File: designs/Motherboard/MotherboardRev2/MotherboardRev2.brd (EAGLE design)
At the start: 160 x 100 mm, 102 parts, among them IC1 PIC24FJ64GB202, IC2 PIC18F26J53SO, J1 Servo 2, J2 Servo 1, J3 Servo 3, J4 Servo 4, J5 Servo 5, J6 Servo 6, Q1 BSS123, Q2 BSS123, Q3 BSS123, Q4 BSS123, U3 LMS8117AMP-3.3

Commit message: More work done on motherboard
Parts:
- removed IC2: PIC18F26J53SO, microchip:SO28W
- removed J1: Servo 2, con-molex:7395-03
- removed J2: Servo 1, con-molex:7395-03
- removed J3: Servo 3, con-molex:7395-03
- removed J4: Servo 4, con-molex:7395-03
- removed J5: Servo 5, con-molex:7395-03
- removed J6: Servo 6, con-molex:7395-03
- added 3.3V, 3.3V(2), 5V, 5V(2): (no value), Son_of_Dark_Powersch:7395-02
- added C33: 10uF, rcl:C0805
- added C34, C35, C36: .1uF, rcl:C0805
- added C37: .1uF, 3-3_fixed:1206
- added C38: 10uF, SparkFun-Capacitors:EIA3216
- added D7: 3_3V_PWR, SparkFun-LED:FKIT-LED-1206
- added D8: 6V_Pwr, SparkFun-LED:FKIT-LED-1206
- added IC3: PIC24FJ64GB202, microchip:QFN28-ML_6X6MM
- added LED10, LED11, LED12: (no value), motherboard_i_autoroute:LED_CHIPLED_1206
- added MOTOR_PWR: (no value), Son_of_Dark_Powersch:7395-04
- added PWR_IN, PWR_IN(2): (no value), Son_of_Dark_Powersch:5569-2
- added R18: 470, rcl:R0805
- added R26: 10k, rcl:R0805
- added R27, R28: 4.7k, rcl:R0805
- added R29, R30, R31: (no value), rcl:M0805
- added R32: 0 ohm, rcl:R1206
- added R33: 4.7K, rcl:R0805
- added R34, R35: (no value), rcl:R0805W
- added SERVO_1, SERVO_10, SERVO_2, SERVO_3, SERVO_4, SERVO_5, SERVO_6, SERVO_7, SERVO_8, SERVO_9: (no value), con-molex:7395-03
- added START_SWITCH: (no value), con-lstb:MA03-1
- added U$10: Switch3, Parts4Class:MC32882_FINAL
- added U$11, U$13, U$14: Switch1, Parts4Class:MC32882_FINAL
- added U$12: Switch2, Parts4Class:MC32882_FINAL
- added U1: LMS8117AMP-3.3, NSC-LMS8117AMP:SOT230P696X180-4N
- C29: value .1uF -> 10uF; device 3-3_fixed:1206 -> SparkFun-Capacitors:EIA3216
- IC1: device microchip:DIL28-3 -> microchip:QFN28-ML_6X6MM
- R17: value 0 ohm -> 4.7K; device rcl:R1206 -> rcl:R0805
- moved R17 371.5 mm to (96.4, 51.1), flipped to the bottom, turned to 270 degrees
- moved C29 351.8 mm to (74.6, 76.9), flipped to the bottom, turned to 90 degrees
- moved PROGRAMMING 256.8 mm to (30.8, 3.73), flipped to the bottom, turned to 0 degrees
- moved D5 227.0 mm to (70.7, 65.7), flipped to the bottom
- moved R15 223.6 mm to (72.4, 61.5), flipped to the bottom
- moved U$5 220.3 mm to (51.8, 14.2), turned to 0 degrees
- moved C24 219.9 mm to (74.2, 65.6), flipped to the bottom
- moved IC1 216.2 mm to (73.3, 47.4), flipped to the bottom
- moved R21 212.7 mm to (94.5, 37.0)
- moved LED5 212.7 mm to (94.3, 31.3)
- moved R22 212.5 mm to (92.4, 37.0)
- moved LED9 212.5 mm to (86.2, 31.3)
- moved R23 212.5 mm to (90.3, 37.0)
- moved R24 212.5 mm to (88.3, 37.0)
- moved R25 212.5 mm to (86.2, 37.0)
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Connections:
- removed net 6V_INPUT1: C28.1, J4.2, J5.2, J6.2
- removed net 6V_INPUT2: C27.1, J1.2, J2.2, J3.2
- removed net BB_PWR_SW: U$3.P9.9
- removed net IO1: IC1.9, R19.1, U$6.P$2, U$6.P$3
- removed net IO2: IC1.2, R20.1, U$7.P$2, U$7.P$3
- removed net VSS: C21.2, C23.C, C24.C, C25.2, C26.2, C27.2, C28.2, D5.C, D6.C, IC1.27, IC1.8, J1.3, J2.3, J3.3, J4.3, J5.3, J6.3, LED5.C, LED6.C, LED7.C, LED8.C, LED9.C, PROGRAMMING.10, PROGRAMMING.9, R19.2, R20.2, U$5.P$1, U$5.P$4, U3.1
- new net BB_PWR_BUTTON: U$1.P9.9, U$13.P$2, U$13.P$3
- new net BB_SYS_RESET: U$1.P9.10, U$14.P$2, U$14.P$3
- new net IO3(1): IC1.7, R29.2
- new net IO4(1): IC1.9, R30.2
- new net IO5(1): IC1.11, R31.2
- new net MCLR'(1): IC1.26, R18.1
- new net MCLR(1): C36.1, R18.2, R26.1, U$10.P$2, U$10.P$3
- new net N$15: LED10.A, R29.1
- new net N$16: LED11.A, R30.1
- new net N$17: LED12.A, R31.1
- new net N$18: C37.1, R32.1, U$1.P9.5, U$1.P9.6
- new net N$21: D8.A, R35.1
- new net N$25: IC3.8
- new net N$31: IC3.14
- new net OC1(1): IC1.23, SERVO_9.1
- new net OC2(1): IC1.22, SERVO_8.1
- new net OC3(1): IC1.21, SERVO_10.1
- new net OC4(1): IC1.19, SERVO_7.1
- new net START_LEFT: START_SWITCH.3, U$1.P9.12
- new net START_RIGHT: START_SWITCH.1, U$1.P9.11
- new net SWITCH_1: IC3.27, R19.1, U$6.P$2, U$6.P$3
- new net SWITCH_2: IC3.6, R20.1, U$7.P$2, U$7.P$3
- new net SWITCH_3: IC1.6, R27.1, U$11.P$2, U$11.P$3
- new net SWITCH_4: IC1.27, R28.1, U$12.P$2, U$12.P$3
- new net VOUT5: 3.3V(2).1, 3.3V.1, C38.A, R34.1, U1.4
- net +5V: now also R32.2; no longer C23.A, R16.2, R17.2, U3.3
- net 3.3V: now also C34.1, C35.1, IC1.10, IC1.25, IC3.10, IC3.25, R17.2, R26.2, R33.2, START_SWITCH.2, U$11.P$1, U$11.P$4, U$12.P$1, U$12.P$4; no longer IC1.13, IC1.28
- net GND: now also 3.3V(2).2, 3.3V.2, 5V(2).2, 5V.2, C21.2, C23.C, C24.C, C25.2, C26.2, C27.2, C28.2, C29.C, C33.2, C34.2, C35.2, C36.2, C37.2, C38.C, D5.C, D6.C, D7.C, D8.C, IC1.24, IC1.5, IC3.24, IC3.5, LED10.C, LED11.C, LED12.C, LED5.C, LED6.C, LED7.C, LED8.C, LED9.C, MOTOR_PWR.1, MOTOR_PWR.4, PROGRAMMING.10, PROGRAMMING.9, PWR_IN(2).1, PWR_IN.1, R19.2, R20.2, R27.2, R28.2, SERVO_1.3, SERVO_10.3, SERVO_2.3, SERVO_3.3, SERVO_4.3, SERVO_5.3, SERVO_6.3, SERVO_7.3, SERVO_8.3, SERVO_9.3, U$10.P$1, U$10.P$4, U$13.P$1, U$13.P$4, U$14.P$1, U$14.P$4, U$5.P$1, U$5.P$4, U1.1, U3.1; no longer C29.2
- net IO3: now also IC3.7; no longer IC1.15
- net IO4: now also IC3.9; no longer IC1.3
- net IO5: now also IC3.11; no longer IC1.10
- net IO6: now also IC3.12; no longer IC1.14
- net IO7: now also IC3.13; no longer IC1.16
- net IO8: now also IC1.28, IC3.28; no longer IC1.17
- net MCLR': now also IC3.26
- net N$11: now also D7.A, R34.2; no longer C29.1, R17.1, U$3.P9.5, U$3.P9.6
- net OC1: now also IC3.23, SERVO_1.1; no longer IC1.25, J2.1
- net OC2: now also IC3.22, SERVO_2.1; no longer IC1.26, J1.1
- net OC3: now also IC3.21, SERVO_3.1; no longer IC1.24, J3.1
- net OC4: now also IC3.19, SERVO_4.1; no longer IC1.22, J4.1
- net OC5: now also IC3.18, SERVO_5.1; no longer IC1.21, J5.1
- net OC6: now also IC3.15, SERVO_6.1; no longer IC1.18, J6.1
- net PGC1: now also IC1.2, IC3.2; no longer IC1.5
- net PGD1: now also IC1.1, IC3.1; no longer IC1.4
- net SCL: now also IC1.4, IC3.4, R33.1; no longer IC1.7
- net SDA: now also IC1.3, IC3.3, R17.1; no longer IC1.6
- net VCC: now also PWR_IN(2).2, PWR_IN.2
- net VOUT1: now also 5V(2).1, 5V.1, C23.A, C29.A, R16.2, R35.2, U1.3, U3.3
- net VOUT2: now also C27.1, SERVO_1.2, SERVO_2.2, SERVO_3.2, SERVO_7.2
- net VOUT3: now also C28.1, C33.1, SERVO_10.2, SERVO_4.2, SERVO_5.2, SERVO_6.2, SERVO_8.2, SERVO_9.2
- net VOUT4: now also MOTOR_PWR.2, MOTOR_PWR.3
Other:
- outline, holes or cut-outs redrawn
- board text removed: "S1"
- board text removed: "S2"
- board text removed: "User LEDs"

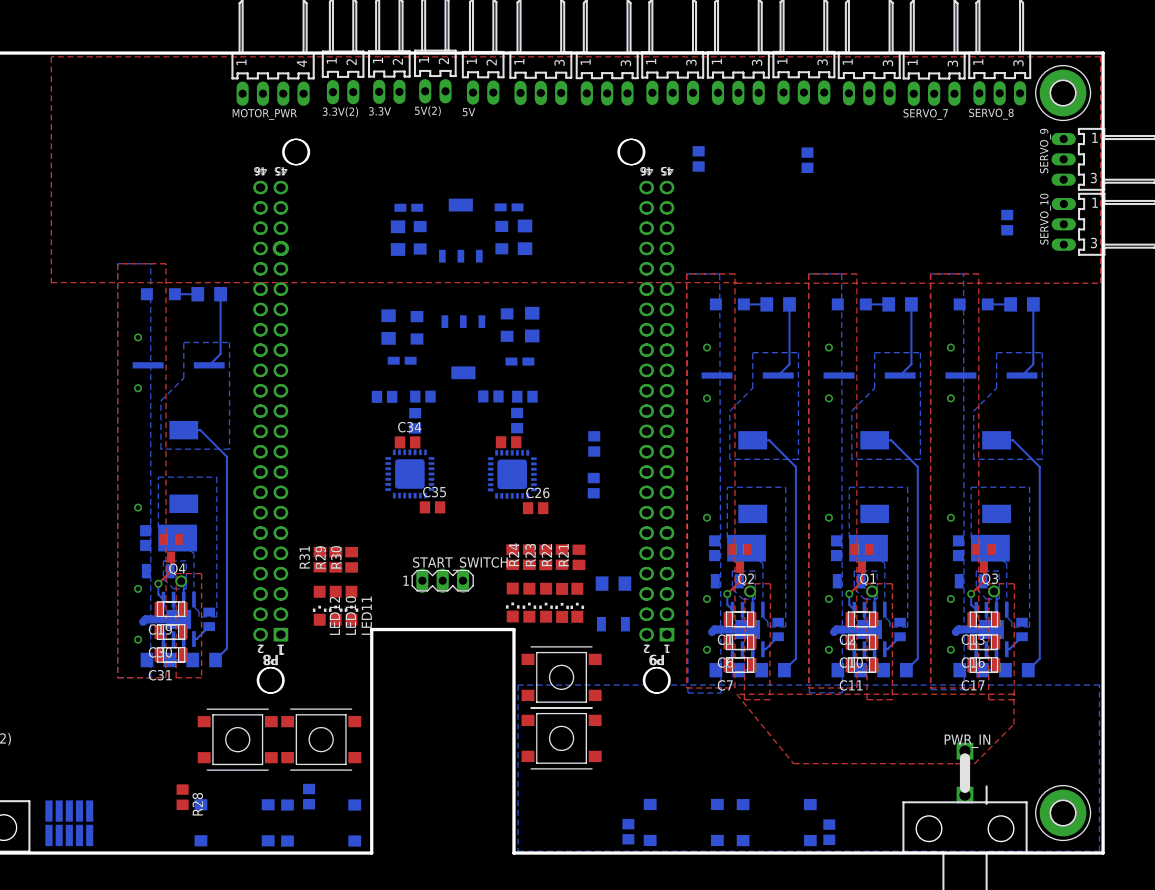
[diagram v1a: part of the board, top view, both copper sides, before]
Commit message: Running traces on motherboard
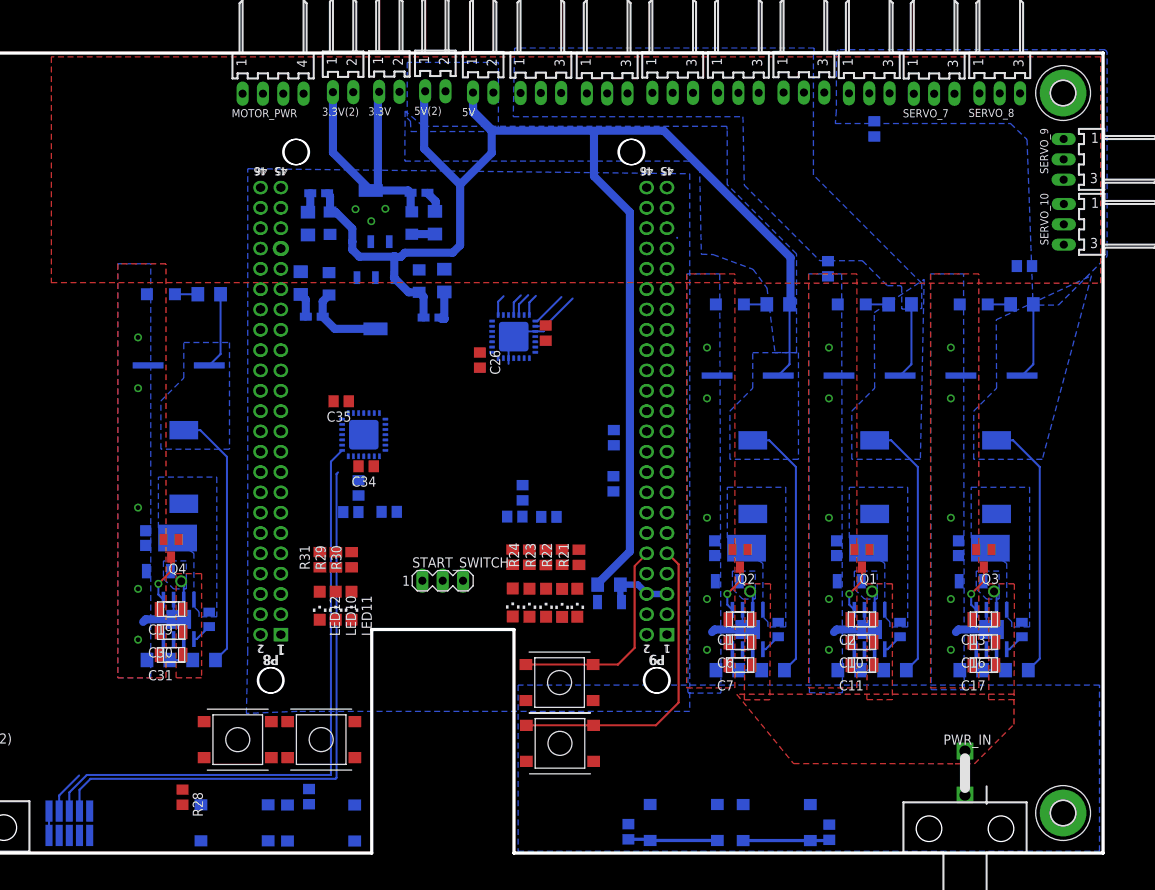
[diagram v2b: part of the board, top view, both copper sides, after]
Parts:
- moved C33 22.3 mm to (131.4, 90.5)
- moved C26 19.8 mm to (82.1, 61.6), turned to 270 degrees
- moved C35 17.5 mm to (64.8, 56.5), turned to 180 degrees
- moved IC3 17.2 mm to (86.3, 64.5), turned to 90 degrees
- moved R26 17.0 mm to (66.0, 42.6), turned to 180 degrees
- moved C21 16.7 mm to (90.7, 42.0), turned to 180 degrees
- moved R14 15.0 mm to (86.5, 42.0), turned to 0 degrees
- moved C25 14.4 mm to (90.3, 65.0), turned to 90 degrees
- moved C36 14.4 mm to (70.8, 42.6), turned to 0 degrees
- moved C28 13.8 mm to (125.6, 73.0)
- moved C23 12.3 mm to (74.5, 71.5)
- moved D6 12.3 mm to (77.7, 71.6)
- moved C24 12.3 mm to (63.2, 71.1)
- moved R15 12.3 mm to (61.4, 67.0)
- moved D5 12.3 mm to (59.7, 71.2)
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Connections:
- removed net +5V: R32.2
- net VOUT1: now also R32.2
- net VOUT2: now also C28.1, SERVO_4.2, SERVO_5.2; no longer SERVO_7.2
- net VOUT3: now also SERVO_7.2; no longer C28.1, SERVO_4.2, SERVO_5.2
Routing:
- net VOUT1: track 42.2 -> 226.0 mm
- net PGD1: track 0.00 -> 77.1 mm
- net PGC1: track 0.00 -> 73.7 mm
- net BB_PWR_BUTTON: track 0.00 -> 39.4 mm
- net VOUT5: track 0.00 -> 34.2 mm
- net BB_SYS_RESET: track 0.00 -> 26.9 mm
- net GND: track 28.2 -> 41.6 mm, vias 20 -> 23
- net SWITCH_1: track 0.00 -> 11.3 mm
- net SWITCH_2: track 0.00 -> 10.9 mm
- net 3.3V: track 0.00 -> 10.3 mm
- net N$18: track 0.00 -> 8.62 mm
- net OC1: track 0.00 -> 6.11 mm
- net MCLR: track 0.00 -> 5.47 mm
- net OC2: track 0.00 -> 4.50 mm
- net N$13: track 0.00 -> 3.99 mm
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
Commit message: Final Motherboard
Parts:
- removed C19, C30, C31, C32: 4.7uF, 5v:1206
- removed C20: 10nF, 5v:0805
- removed C22: 330uF, 5v:SM_RADIAL_10AMM
- removed C33: 10uF, rcl:C0805
- removed C34, C35, C36: .1uF, rcl:C0805
- removed D4: PDS760-13, 5v:POWERDI5
- removed D6, D8: 6V_Pwr, SparkFun-LED:FKIT-LED-1206
- removed IC1: PIC24FJ64GB202, microchip:QFN28-ML_6X6MM
- removed L4: (no value), WE-HCC:WE-HCC_1090
- removed LED10, LED11, LED12: (no value), motherboard_i_autoroute:LED_CHIPLED_1206
- removed LED3: (no value), led:SML1206
- removed MOTOR_PWR: (no value), Son_of_Dark_Powersch:7395-04
- removed PWR_IN(2): (no value), Son_of_Dark_Powersch:5569-2
- removed Q4: BSS123, transistor-small-signal:SOT23
- removed R12: 10k, rcl:R1206
- removed R16, R35: (no value), rcl:R0805W
- removed R18: 470, rcl:R0805
- removed R26: 10k, rcl:R0805
- removed R27, R28: 4.7k, rcl:R0805
- removed R29, R30, R31: (no value), rcl:M0805
- removed SERVO_10, SERVO_7, SERVO_8, SERVO_9: (no value), con-molex:7395-03
- removed U$10: Switch3, Parts4Class:MC32882_FINAL
- removed U$11: Switch1, Parts4Class:MC32882_FINAL
- removed U$12: Switch2, Parts4Class:MC32882_FINAL
- removed U$3: BEAGLE_BONE_BLACK_CAPE, SparkFun-Boards:BEAGLE_BONE_BLACK_CAPE
- removed U$9: TPS5450DDAR, 5v:R-PDSO-G8
- added 3.3V(2)1, 3.3V1, 5V(2)1, 5V1: (no value), Son_of_Dark_Powersch:7395-02
- C1, C10, C11, C12, C13, C16, C17, C18, C2, C6, C7, C8: device 5v:1206 -> rcl:C0805
- C21, C25, C26: device rcl:C0805 -> rcl:C0402
- C37: device 3-3_fixed:1206 -> rcl:C0402
- LED5, LED6, LED7, LED8, LED9: device motherboard_i_autoroute:LED_CHIPLED_1206 -> led:CHIPLED-0603-TTW
- R10: value 10k -> (none); device rcl:R1206 -> rcl:R0402
- R11, R32: device rcl:R1206 -> rcl:R0402
- R13, R14, R17, R19, R20, R33: device rcl:R0805 -> rcl:R0402
- R21, R22, R23, R24, R25: device rcl:M0805 -> rcl:R0402
- moved PROGRAMMING 71.8 mm to (98.0, 29.0), flipped to the top
- moved SERVO_1 64.9 mm to (152.4, 78.2), turned to 90 degrees
- moved SERVO_2 54.9 mm to (152.2, 86.4), turned to 90 degrees
- moved U$5 52.7 mm to (103.9, 6.21), flipped to the bottom, turned to 270 degrees
- moved SERVO_3 39.1 mm to (145.0, 90.8)
- moved R10 38.5 mm to (85.3, 32.0), flipped to the top
- moved U$14 37.9 mm to (126.8, 6.13), flipped to the bottom, turned to 270 degrees
- moved R20 35.0 mm to (91.8, 11.1), flipped to the top, turned to 0 degrees
- moved U$7 32.2 mm to (90.8, 19.0), flipped to the top, turned to 270 degrees
- moved R11 29.0 mm to (69.9, 31.8), flipped to the top, turned to 0 degrees
- moved U$13 27.2 mm to (118.3, 6.17), flipped to the bottom, turned to 270 degrees
- moved SERVO_4 22.9 mm to (136.9, 90.7)
- moved R14 20.6 mm to (98.0, 25.0), flipped to the top, turned to 180 degrees
- moved U$6 17.7 mm to (98.4, 18.9), flipped to the top, turned to 270 degrees
- moved D7 16.1 mm to (60.7, 82.1), flipped to the top
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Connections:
- removed net BOOT4: C20.1, U$9.1
- removed net EN4: Q4.1
- removed net ENA_4: Q4.3, U$9.5
- removed net IO3(1): IC1.7, R29.2
- removed net IO4(1): IC1.9, R30.2
- removed net IO5(1): IC1.11, R31.2
- removed net MCLR'(1): IC1.26, R18.1
- removed net MCLR(1): C36.1, R18.2, R26.1, U$10.P$2, U$10.P$3
- removed net N$12: U$3.P8.7
- removed net N$13: D6.A, R16.1
- removed net N$14: U$3.P8.8
- removed net N$15: LED10.A, R29.1
- removed net N$16: LED11.A, R30.1
- removed net N$17: LED12.A, R31.1
- removed net N$21: D8.A, R35.1
- removed net N$4: LED3.A, R12.1
- removed net OC1(1): IC1.23, SERVO_9.1
- removed net OC2(1): IC1.22, SERVO_8.1
- removed net OC3(1): IC1.21, SERVO_10.1
- removed net OC4(1): IC1.19, SERVO_7.1
- removed net PH4: C20.2, D4.3, L4.1, U$9.8
- removed net SWITCH_3: IC1.6, R27.1, U$11.P$2, U$11.P$3
- removed net SWITCH_4: IC1.27, R28.1, U$12.P$2, U$12.P$3
- removed net VOUT4: C22.1, L4.2, MOTOR_PWR.2, MOTOR_PWR.3, R10.2, R12.2
- removed net VSNS4: R10.1, R11.2, U$9.4
- net 3.3V: no longer C34.1, C35.1, IC1.10, IC1.25, R26.2, U$11.P$1, U$11.P$4, U$12.P$1, U$12.P$4
- net GND: now also 3.3V(2)1.2, 3.3V1.2, 5V(2)1.2, 5V1.2, LED5.C@1, LED6.C@1, LED7.C@1, LED8.C@1, LED9.C@1, R10.1; no longer C19.1, C22.2, C30.1, C31.1, C32.1, C33.2, C34.2, C35.2, C36.2, D4.1, D6.C, D8.C, IC1.24, IC1.5, LED10.C, LED11.C, LED12.C, LED3.C, LED5.C, LED6.C, LED7.C, LED8.C, LED9.C, MOTOR_PWR.1, MOTOR_PWR.4, PWR_IN(2).1, Q4.2, R27.2, R28.2, SERVO_10.3, SERVO_7.3, SERVO_8.3, SERVO_9.3, U$10.P$1, U$10.P$4, U$3.P8.1, U$3.P8.2, U$3.P9.1, U$3.P9.2, U$3.P9.43, U$3.P9.44, U$3.P9.45, U$3.P9.46, U$9.6, U$9.9
- net IO3: now also R25.2; no longer R21.2
- net IO4: now also R24.2; no longer R25.2
- net IO5: now also R23.2; no longer R24.2
- net IO7: now also R21.2; no longer R23.2
- net IO8: no longer IC1.28
- net N$5: now also LED5.A@1; no longer LED5.A
- net N$6: now also LED6.A@1; no longer LED6.A
- net N$7: now also LED7.A@1; no longer LED7.A
- net N$8: now also LED8.A@1; no longer LED8.A
- net N$9: now also LED9.A@1; no longer LED9.A
- net OC1: now also SERVO_6.1; no longer SERVO_1.1
- net OC2: now also SERVO_5.1; no longer SERVO_2.1
- net OC3: now also SERVO_4.1; no longer SERVO_3.1
- net OC4: now also SERVO_3.1; no longer SERVO_4.1
- net OC5: now also SERVO_2.1; no longer SERVO_5.1
- net OC6: now also SERVO_1.1; no longer SERVO_6.1
- net PGC1: no longer IC1.2
- net PGD1: no longer IC1.1
- net SCL: no longer IC1.4
- net SDA: no longer IC1.3
- net START_LEFT: now also R10.2
- net START_RIGHT: now also R11.2
- net VCC: no longer C19.2, C30.2, C31.2, C32.2, PWR_IN(2).2, U$9.7
- net VOUT1: now also 5V(2)1.1, 5V1.1; no longer R16.2, R35.2
- net VOUT2: now also SERVO_6.2; no longer C27.1, SERVO_1.2, SERVO_2.2, SERVO_3.2
- net VOUT3: now also C27.1, SERVO_1.2, SERVO_2.2, SERVO_3.2; no longer C33.1, SERVO_10.2, SERVO_6.2, SERVO_7.2, SERVO_8.2, SERVO_9.2
- net VOUT5: now also 3.3V(2)1.1, 3.3V1.1
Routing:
- net 3.3V: track 10.3 -> 145.3 mm, vias 0 -> 5
- net OC6: track 2.63 -> 124.3 mm, vias 0 -> 1
- net VOUT1: track 226.0 -> 109.9 mm
- net OC5: track 2.83 -> 108.5 mm, vias 0 -> 1
- net OC4: track 2.97 -> 98.2 mm, vias 0 -> 1
- net OC3: track 2.74 -> 90.0 mm, vias 0 -> 1
- net OC2: track 4.50 -> 81.5 mm, vias 0 -> 1
- net OC1: track 6.11 -> 65.6 mm, vias 0 -> 1
- net PGD1: track 77.1 -> 32.0 mm, vias 0 -> 1
- net SWITCH_1: track 11.3 -> 55.7 mm, vias 0 -> 1
- net PGC1: track 73.7 -> 30.5 mm, vias 0 -> 1
- net VOUT4: track 42.2 -> 0.00 mm
- net START_RIGHT: track 0.00 -> 39.8 mm
- net VOUT5: track 34.2 -> 73.3 mm
- net SWITCH_2: track 10.9 -> 47.9 mm, vias 0 -> 1
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- removed copper zone on layer 16, net PH4
- removed copper zone on layer 16, net VOUT4
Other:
- board text added: "BBB Power Off"
- board text added: "BBB Reset"
- board text added: "PIC Reset"
